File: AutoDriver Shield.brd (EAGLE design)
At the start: 73.7 x 49.5 mm, 44 parts, among them U1 MAX489CSD, U2 MAX489CSD, U3 MAX489CSD, U4 MAX489CSD, U5 LM46001, U6 74AHC1G14DBV

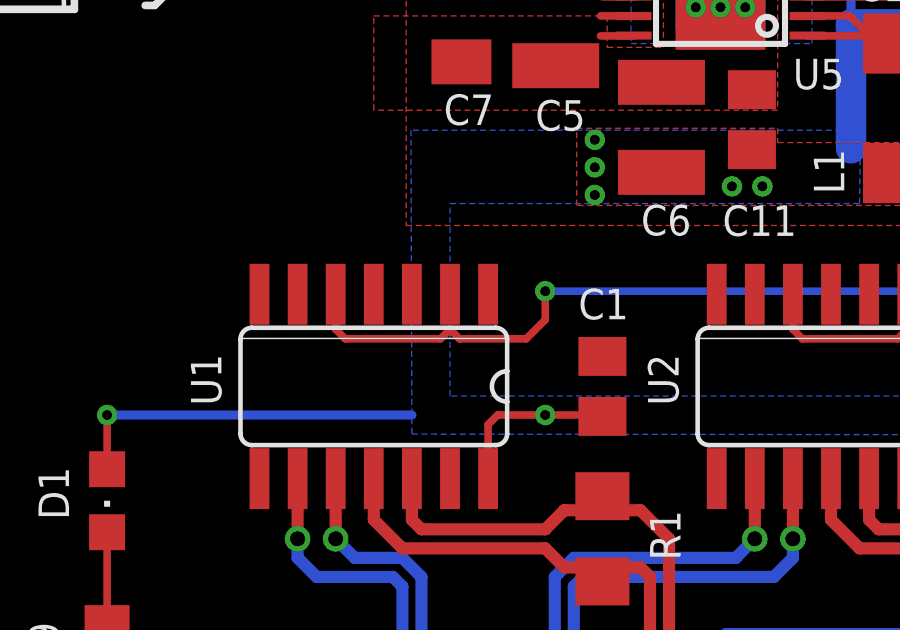
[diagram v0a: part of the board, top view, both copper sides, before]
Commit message: Added missing trace connecting U1 pin 2 to SCK signals.
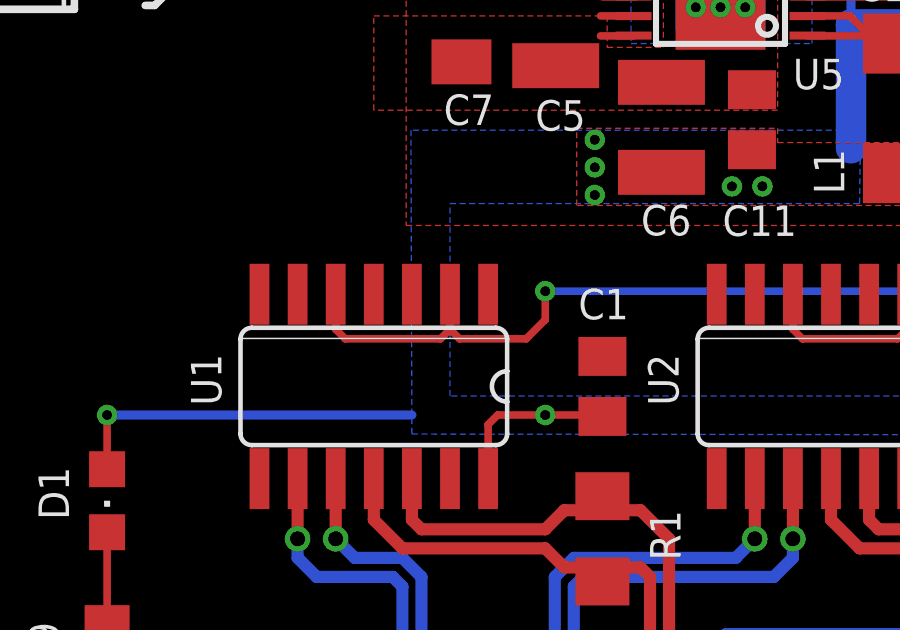
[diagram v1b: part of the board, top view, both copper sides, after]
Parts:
- C1, C13, C2, C3, C4: value 0.1 -> 0.1uf
- U1, U2, U3, U4: value MAX489CSD -> MAX14786E
- U6: value 74AHC1G14DBV -> 74AHC1G14
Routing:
- net SCK: track 57.4 -> 58.3 mm
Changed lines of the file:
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@@
 <element name="STANDOFF3" library="SparkFun" package="STAND-OFF" value="STAND-OFF" x="2.54" y="2.54" locked="yes" rot="R90"/>
 <element name="STANDOFF4" library="SparkFun" package="STAND-OFF" value="STAND-OFF" x="2.54" y="46.99" locked="yes" rot="R90"/>
-<element name="C4" library="resistor" package="C0805K" value="0.1" x="67.31" y="19.05" smashed="yes" rot="R90">
+<element name="C4" library="resistor" package="C0805K" value="0.1uf" x="67.31" y="19.05" smashed="yes" rot="R90">
 <attribute name="NAME" x="66.51" y="21.2875" size="1.016" layer="25" font="vector" ratio="10"/>
 </element>
@@
 <attribute name="NAME" x="60.325" y="12.065" size="1.016" layer="25" font="vector" ratio="10"/>
 </element>
-<element name="U4" library="maxim" package="SO14" value="MAX489CSD" x="59.69" y="19.05" smashed="yes" rot="R180">
+<element name="U4" library="maxim" package="SO14" value="MAX14786E" x="59.69" y="19.05" smashed="yes" rot="R180">
 <attribute name="OC_NEWARK" value="34C3923" x="68.58" y="15.24" size="1.778" layer="27" rot="R180" display="off"/>
 <attribute name="MPN" value="MAX489CSD" x="68.58" y="15.24" size="1.778" layer="27" rot="R180" display="off"/>
@@
 <attribute name="NAME" x="53.5305" y="19.939" size="1.016" layer="25" font="vector" ratio="10" rot="R270"/>
 </element>
-<element name="C2" library="resistor" package="C0805K" value="0.1" x="36.83" y="19.05" smashed="yes" rot="R90">
+<element name="C2" library="resistor" package="C0805K" value="0.1uf" x="36.83" y="19.05" smashed="yes" rot="R90">
 <attribute name="NAME" x="36.03" y="21.2875" size="1.016" layer="25" font="vector" ratio="10"/>
 </element>
@@
 <attribute name="NAME" x="38.4175" y="14.9225" size="1.016" layer="25" font="vector" ratio="10" rot="R270"/>
 </element>
-<element name="U2" library="maxim" package="SO14" value="MAX489CSD" x="29.21" y="19.05" smashed="yes" rot="R180">
+<element name="U2" library="maxim" package="SO14" value="MAX14786E" x="29.21" y="19.05" smashed="yes" rot="R180">
 <attribute name="OC_NEWARK" value="34C3923" x="38.1" y="15.24" size="1.778" layer="27" rot="R180" display="off"/>
 <attribute name="MPN" value="MAX489CSD" x="38.1" y="15.24" size="1.778" layer="27" rot="R180" display="off"/>
@@
 <attribute name="NAME" x="23.114" y="20.1295" size="1.016" layer="25" font="vector" ratio="10" rot="R270"/>
 </element>
-<element name="C3" library="resistor" package="C0805K" value="0.1" x="52.07" y="19.05" smashed="yes" rot="R90">
+<element name="C3" library="resistor" package="C0805K" value="0.1uf" x="52.07" y="19.05" smashed="yes" rot="R90">
 <attribute name="NAME" x="51.27" y="21.2875" size="1.016" layer="25" font="vector" ratio="10"/>
 </element>
@@
 <attribute name="NAME" x="53.6575" y="14.9225" size="1.016" layer="25" font="vector" ratio="10" rot="R270"/>
 </element>
-<element name="U3" library="maxim" package="SO14" value="MAX489CSD" x="44.45" y="19.05" smashed="yes" rot="R180">
+<element name="U3" library="maxim" package="SO14" value="MAX14786E" x="44.45" y="19.05" smashed="yes" rot="R180">
 <attribute name="OC_NEWARK" value="34C3923" x="53.34" y="15.24" size="1.778" layer="27" rot="R180" display="off"/>
 <attribute name="MPN" value="MAX489CSD" x="53.34" y="15.24" size="1.778" layer="27" rot="R180" display="off"/>
@@
 <attribute name="NAME" x="38.354" y="20.1295" size="1.016" layer="25" font="vector" ratio="10" rot="R270"/>
 </element>
-<element name="C1" library="resistor" package="C0805K" value="0.1" x="21.59" y="19.05" smashed="yes" rot="R90">
+<element name="C1" library="resistor" package="C0805K" value="0.1uf" x="21.59" y="19.05" smashed="yes" rot="R90">
 <attribute name="NAME" x="20.79" y="21.2875" size="1.016" layer="25" font="vector" ratio="10"/>
 </element>
@@
 <attribute name="NAME" x="23.1775" y="14.9225" size="1.016" layer="25" font="vector" ratio="10" rot="R270"/>
 </element>
-<element name="U1" library="maxim" package="SO14" value="MAX489CSD" x="13.97" y="19.05" smashed="yes" rot="R180">
+<element name="U1" library="maxim" package="SO14" value="MAX14786E" x="13.97" y="19.05" smashed="yes" rot="R180">
 <attribute name="OC_NEWARK" value="34C3923" x="22.86" y="15.24" size="1.778" layer="27" rot="R180" display="off"/>
 <attribute name="MPN" value="MAX489CSD" x="22.86" y="15.24" size="1.778" layer="27" rot="R180" display="off"/>
@@
 <attribute name="NAME" x="17.97675" y="28.78225" size="1.016" layer="25" font="vector" ratio="10" rot="R180"/>
 </element>
-<element name="U6" library="74xx-little-us" package="SOT23-5" value="74AHC1G14DBV" x="58.42" y="28.575" smashed="yes" rot="R270">
+<element name="U6" library="74xx-little-us" package="SOT23-5" value="74AHC1G14" x="58.42" y="28.575" smashed="yes" rot="R270">
 <attribute name="NAME" x="57.5945" y="25.5905" size="1.016" layer="25" font="vector" ratio="10"/>
 </element>
@@
 <attribute name="NAME" x="28.067" y="25.0825" size="1.016" layer="25" font="vector" ratio="10" rot="R180"/>
 </element>
-<element name="C13" library="resistor" package="C0805K" value="0.1" x="58.42" y="33.02" smashed="yes">
+<element name="C13" library="resistor" package="C0805K" value="0.1uf" x="58.42" y="33.02" smashed="yes">
 <attribute name="NAME" x="57.1025" y="34.2125" size="1.016" layer="25" font="vector" ratio="10"/>
 </element>
@@
 <wire x1="16.8275" y1="20.6375" x2="16.51" y2="20.955" width="0.254" layer="1"/>
 <via x="19.685" y="22.225" extent="1-16" drill="0.3302"/>
-<wire x1="16.51" y1="20.955" x2="16.51" y2="22.1234" width="0" layer="19" extent="1-1"/>
+<wire x1="16.51" y1="20.955" x2="16.51" y2="21.9075" width="0.254" layer="1"/>
+<wire x1="16.51" y1="21.9075" x2="16.51" y2="22.1234" width="0" layer="19" extent="1-1"/>
 <wire x1="12.7" y1="22.1234" x2="12.7" y2="22.225" width="0" layer="19" extent="1-1"/>
 </signal>

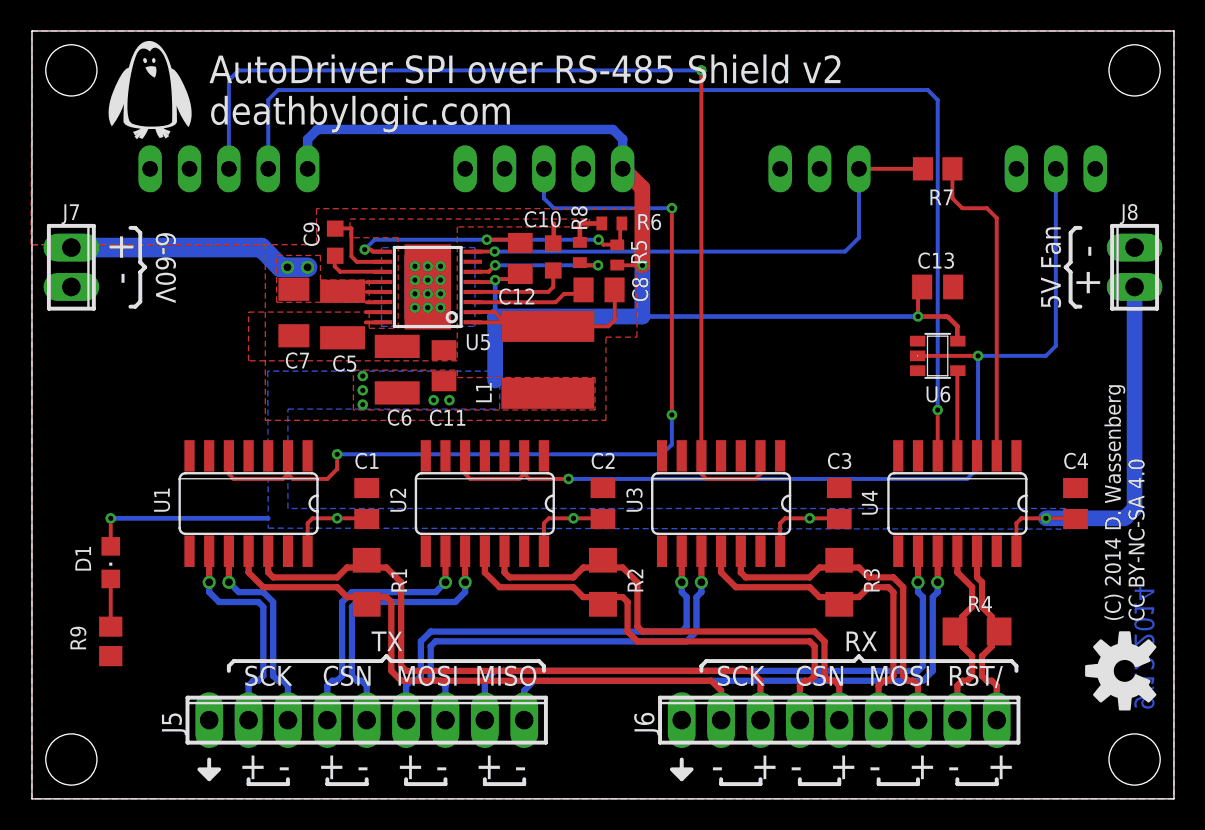
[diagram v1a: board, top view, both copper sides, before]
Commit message: Removed Non-Commercial License; Updated website address.
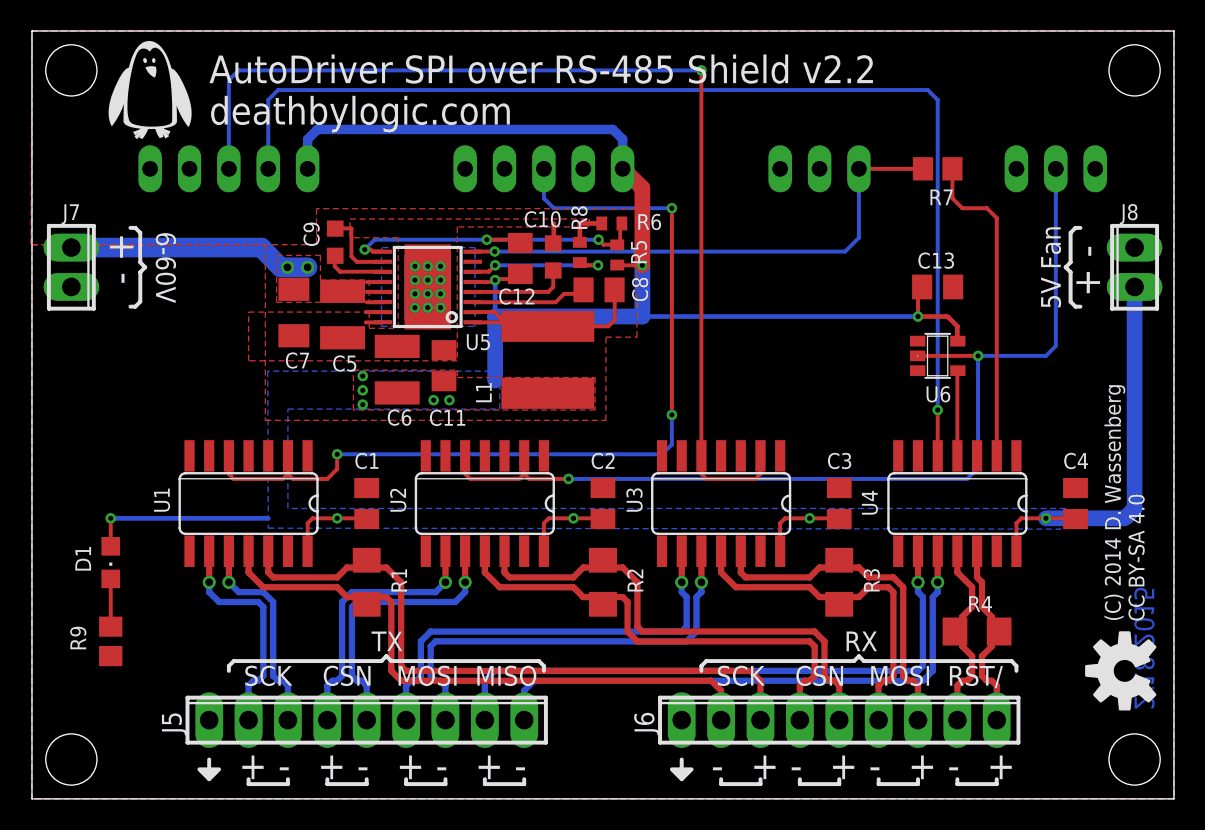
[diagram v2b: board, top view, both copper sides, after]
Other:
- board text added: "(C) 2014 D. Wassenberg CC BY-SA 4.0"
- board text added: "2/18/2015"
- board text added: "AutoDriver SPI over RS-485 Shield v2.2 deathbylogic.com"
- board text removed: "(C) 2014 D. Wassenberg CC BY-NC-SA 4.0"
- board text removed: "9/12/2014"
- board text removed: "AutoDriver SPI over RS-485 Shield v2 deathbylogic.com"
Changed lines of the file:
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@@
 <layer number="21" name="tPlace" color="7" fill="1" visible="yes" active="yes"/>
 <layer number="22" name="bPlace" color="7" fill="1" visible="yes" active="yes"/>
-<layer number="23" name="tOrigins" color="15" fill="1" visible="yes" active="yes"/>
-<layer number="24" name="bOrigins" color="15" fill="1" visible="yes" active="yes"/>
+<layer number="23" name="tOrigins" color="15" fill="1" visible="no" active="yes"/>
+<layer number="24" name="bOrigins" color="15" fill="1" visible="no" active="yes"/>
 <layer number="25" name="tNames" color="7" fill="1" visible="yes" active="yes"/>
 <layer number="26" name="bNames" color="7" fill="1" visible="yes" active="yes"/>
@@
 <wire x1="73.66" y1="49.53" x2="0" y2="49.53" width="0" layer="20"/>
 <wire x1="0" y1="49.53" x2="0" y2="0" width="0" layer="20"/>
-<text x="11.43" y="43.4975" size="1.778" layer="21" font="vector" ratio="10">AutoDriver SPI over RS-485 Shield v2
+<text x="11.43" y="43.4975" size="1.778" layer="21" font="vector" ratio="10">AutoDriver SPI over RS-485 Shield v2.2
 deathbylogic.com</text>
 <text x="28.575" y="7.3025" size="1.27" layer="21" font="vector" ratio="10">MISO</text>
@@
 <wire x1="67.31" y1="36.83" x2="67.6275" y2="36.83" width="0.254" layer="21"/>
 <text x="66.3575" y="34.29" size="1.27" layer="21" font="vector" ratio="10" rot="SR90" align="bottom-center">5V Fan</text>
-<text x="71.12" y="5.715" size="1.27" layer="16" font="vector" ratio="15" rot="MR90">9/12/2014</text>
+<text x="71.12" y="5.715" size="1.27" layer="16" font="vector" ratio="15" rot="MR90">2/18/2015</text>
 <text x="71.755" y="11.43" size="1.016" layer="21" font="vector" rot="R90">(C) 2014 D. Wassenberg
-CC BY-NC-SA 4.0</text>
+CC BY-SA 4.0</text>
 </plain>
 <attributes>
